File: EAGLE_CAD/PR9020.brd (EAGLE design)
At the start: 70 x 70 mm, 73 parts

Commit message: PR9020 Gerbers
PR9020 Gerbers, organized folders
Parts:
- moved MARK1 0.94 mm to (16.2, 8.50)
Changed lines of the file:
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@@
 <rectangle x1="35.3949" y1="12.6365" x2="35.4711" y2="12.6619" layer="26" rot="R180"/>
 <rectangle x1="35.4203" y1="12.6619" x2="35.5981" y2="12.6873" layer="26" rot="R180"/>
-<text x="64" y="35" size="0.8128" layer="26" font="vector" ratio="18" rot="MR270" align="center">PR9020
+<text x="64" y="35" size="0.8128" layer="26" font="vector" ratio="22" rot="MR270" align="center">PR9020
 Born + tuned in Brooklyn
 http://thepublicrad.io</text>
@@
 </element>
 <element name="R21" library="PR_Parts_Library" package="0603_CPL" value="12K" x="41.7" y="8.7" smashed="yes" rot="R180">
-<attribute name="NAME" x="43.551" y="8.389" size="0.8128" layer="25" font="vector" ratio="16"/>
+<attribute name="NAME" x="43.851" y="8.389" size="0.8128" layer="25" font="vector" ratio="16"/>
 <attribute name="VALUE" x="42.589" y="10.732" size="1.27" layer="27" rot="R180"/>
 <attribute name="MFG_PN" value="RC0603FR-0712KL" x="41.7" y="8.7" size="1.778" layer="27" rot="R180" display="off"/>
@@
 </element>
 <element name="C21" library="PR_Parts_Library" package="0603_CPL" value=".22uF" x="41.9" y="7.1" smashed="yes" rot="R180">
-<attribute name="NAME" x="43.861" y="6.762" size="0.8128" layer="25" font="vector" ratio="16"/>
+<attribute name="NAME" x="43.761" y="6.762" size="0.8128" layer="25" font="vector" ratio="16"/>
 <attribute name="VALUE" x="42.789" y="9.132" size="1.27" layer="27" rot="R180"/>
 <attribute name="MFG_PN" value="C1608X7R1C224K080AC" x="41.9" y="7.1" size="1.778" layer="27" rot="R180" display="off"/>
@@
 </element>
 <element name="C23" library="PR_Parts_Library" package="0603_CPL" value=".1uF" x="31.1" y="9.1" smashed="yes" rot="R180">
-<attribute name="NAME" x="26.8855" y="8.872" size="0.8128" layer="25" font="vector" ratio="16"/>
+<attribute name="NAME" x="27.0855" y="8.972" size="0.8128" layer="25" font="vector" ratio="16"/>
 <attribute name="VALUE" x="32.116" y="10.497" size="0.4064" layer="27" rot="R180"/>
 <attribute name="MFG_PN" value="CL10B104KB8SFNC" x="31.1" y="9.1" size="1.778" layer="27" rot="R180" display="off"/>
@@
 </element>
 <element name="FB2" library="PR_Parts_Library" package="0805_ADAFRUIT" value="" x="31.1" y="12.1" smashed="yes" rot="R180">
-<attribute name="NAME" x="26.985" y="11.88" size="0.8128" layer="25" font="vector" ratio="16"/>
+<attribute name="NAME" x="27.185" y="11.78" size="0.8128" layer="25" font="vector" ratio="16"/>
 <attribute name="VALUE" x="31.735" y="14.64" size="1.27" layer="27" rot="R180"/>
 <attribute name="MFG_PN" value="HI0805R800R-10" x="31.1" y="12.1" size="1.778" layer="27" rot="R180" display="off"/>
@@
 </element>
 <element name="FB3" library="PR_Parts_Library" package="0805_ADAFRUIT" value="" x="31.11" y="5.94" smashed="yes">
-<attribute name="NAME" x="27.275" y="5.32" size="0.8128" layer="25" font="vector" ratio="16"/>
+<attribute name="NAME" x="27.075" y="5.32" size="0.8128" layer="25" font="vector" ratio="16"/>
 <attribute name="VALUE" x="30.475" y="3.4" size="1.27" layer="27"/>
 <attribute name="MFG_PN" value="HI0805R800R-10" x="31.11" y="5.94" size="1.778" layer="27" display="off"/>
@@
 <attribute name="MFG_PN" value="DNP" x="39" y="68" size="1.778" layer="28" rot="MR0" display="off"/>
 </element>
-<element name="MARK1" library="PR_Parts_Library" package="FIDUCIAL_1MM" value="" x="17" y="9">
-<attribute name="MFG_PN" value="DNP" x="17" y="9" size="1.778" layer="27" display="off"/>
+<element name="MARK1" library="PR_Parts_Library" package="FIDUCIAL_1MM" value="" x="16.2" y="8.5">
+<attribute name="MFG_PN" value="DNP" x="16.2" y="8.5" size="1.778" layer="27" display="off"/>
 </element>
 <element name="MARK2" library="PR_Parts_Library" package="FIDUCIAL_1MM" value="" x="33" y="67">
@@
 </element>
 <element name="C24" library="PR_Parts_Library" package="0603_CPL" value="1uF" x="31.1" y="10.3" smashed="yes" rot="R180">
-<attribute name="NAME" x="27.005" y="10.565" size="0.8128" layer="25" font="vector" ratio="16"/>
+<attribute name="NAME" x="27.105" y="10.565" size="0.8128" layer="25" font="vector" ratio="16"/>
 <attribute name="VALUE" x="31.735" y="12.205" size="1.27" layer="27" rot="R180"/>
 <attribute name="MFG_PN" value="CL10B105KP8NNNC" x="31.1" y="10.3" size="1.778" layer="27" rot="R180" display="off"/>
@@
 <via x="46.35" y="40.8" extent="1-16" drill="0.6"/>
 <via x="43.15" y="4.1" extent="1-16" drill="0.6"/>
-<via x="16.09" y="6.96" extent="1-16" drill="0.6"/>
+<via x="16.79" y="6.66" extent="1-16" drill="0.6"/>
 <via x="21.8" y="13.9" extent="1-16" drill="0.6"/>
 <via x="28.55" y="23.6" extent="1-16" drill="0.6"/>

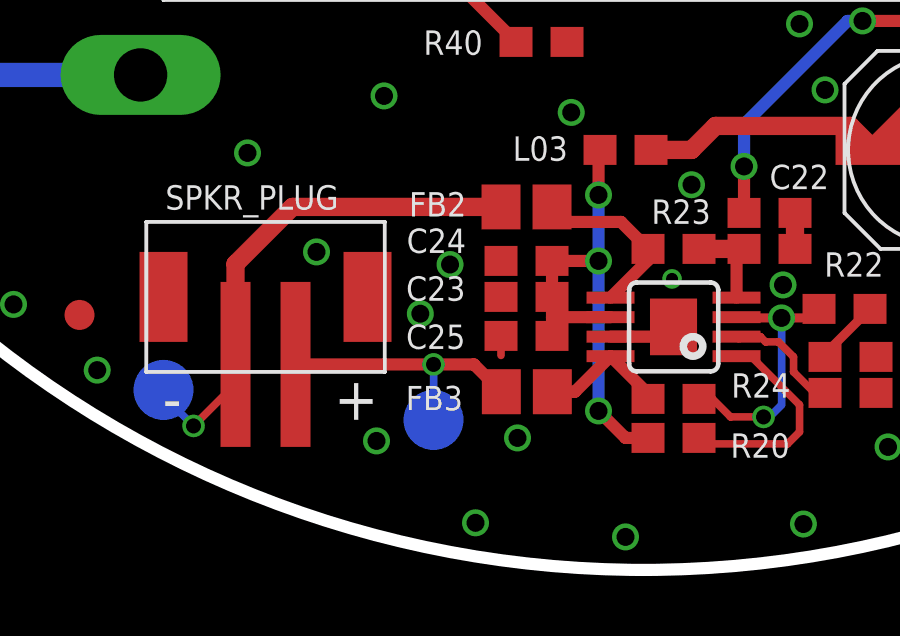
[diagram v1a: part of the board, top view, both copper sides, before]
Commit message: Updated MFG#s
Changed ferrite beads to 0 ohm resistors
Removed ‘dnp’ from R40
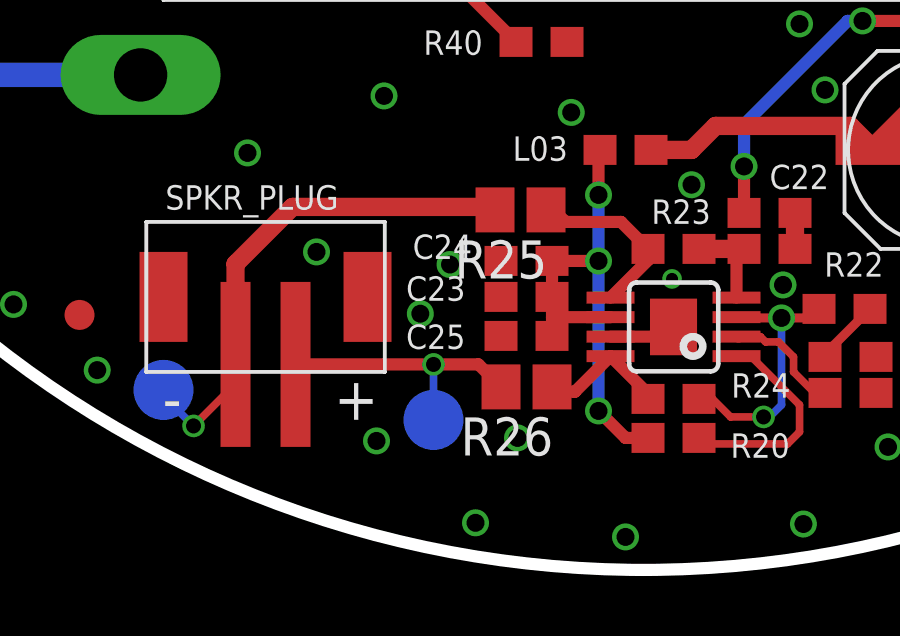
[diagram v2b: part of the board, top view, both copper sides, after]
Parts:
- removed FB2, FB3: (no value), PR_Parts_Library:0805_ADAFRUIT
- added R25, R26: 0 ohm, PR_Parts_Library:0805_ADAFRUIT
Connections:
- net N$11: now also R26.1; no longer FB3.2
- net N$4: now also R25.1; no longer FB2.1
- net SPK_OUT+: now also R25.2; no longer FB2.2
- net SPK_OUT-: now also R26.2; no longer FB3.1
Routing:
- net GND: track 16.7 -> 16.1 mm
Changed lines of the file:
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@@
 <?xml version="1.0" encoding="utf-8"?>
 <!DOCTYPE eagle SYSTEM "eagle.dtd">
-<eagle version="6.6.0">
+<eagle version="7.2.0">
 <drawing>
 <settings>
@@
 <pass name="Default">
 <param name="RoutingGrid" value="50mil"/>
+<param name="AutoGrid" value="1"/>
+<param name="Efforts" value="0"/>
+<param name="TopRouterVariant" value="1"/>
 <param name="tpViaShape" value="round"/>
 <param name="PrefDir.1" value="|"/>
@@
 <attribute name="MFG_PN" value="2 of BK92 - supplied by CL Labs" x="35" y="16.5" size="1.778" layer="28" rot="MR0" display="off"/>
 </element>
-<element name="FB2" library="PR_Parts_Library" package="0805_ADAFRUIT" value="" x="31.1" y="12.1" smashed="yes" rot="R180">
-<attribute name="NAME" x="27.185" y="11.78" size="0.8128" layer="25" font="vector" ratio="16"/>
-<attribute name="VALUE" x="31.735" y="14.64" size="1.27" layer="27" rot="R180"/>
-<attribute name="MFG_PN" value="HI0805R800R-10" x="31.1" y="12.1" size="1.778" layer="27" rot="R180" display="off"/>
-<attribute name="CURRENT" value="2A" x="31.1" y="12.1" size="1.778" layer="27" rot="R180" display="off"/>
-<attribute name="TOL" value="" x="31.1" y="12.1" size="1.778" layer="27" rot="R180" display="off"/>
-<attribute name="DCR" value="45m" x="31.1" y="12.1" size="1.778" layer="27" rot="R180" display="off"/>
-</element>
-<element name="FB3" library="PR_Parts_Library" package="0805_ADAFRUIT" value="" x="31.11" y="5.94" smashed="yes">
-<attribute name="NAME" x="27.075" y="5.32" size="0.8128" layer="25" font="vector" ratio="16"/>
-<attribute name="VALUE" x="30.475" y="3.4" size="1.27" layer="27"/>
-<attribute name="MFG_PN" value="HI0805R800R-10" x="31.11" y="5.94" size="1.778" layer="27" display="off"/>
-<attribute name="CURRENT" value="2A" x="31.11" y="5.94" size="1.778" layer="27" display="off"/>
-<attribute name="TOL" value="" x="31.11" y="5.94" size="1.778" layer="27" display="off"/>
-<attribute name="DCR" value="45m" x="31.11" y="5.94" size="1.778" layer="27" display="off"/>
-</element>
 <element name="R30" library="PR_Parts_Library" package="0603_CPL" value="10K" x="47.3" y="52" smashed="yes">
 <attribute name="NAME" x="49.111" y="51.089" size="0.8128" layer="25" font="vector" ratio="16"/>
@@
 </element>
 <element name="C24" library="PR_Parts_Library" package="0603_CPL" value="1uF" x="31.1" y="10.3" smashed="yes" rot="R180">
-<attribute name="NAME" x="27.105" y="10.565" size="0.8128" layer="25" font="vector" ratio="16"/>
+<attribute name="NAME" x="27.305" y="10.365" size="0.8128" layer="25" font="vector" ratio="16"/>
 <attribute name="VALUE" x="31.735" y="12.205" size="1.27" layer="27" rot="R180"/>
 <attribute name="MFG_PN" value="CL10B105KP8NNNC" x="31.1" y="10.3" size="1.778" layer="27" rot="R180" display="off"/>
@@
 <attribute name="VALUE" x="61.66" y="51.27" size="1.27" layer="27" rot="R270"/>
 <attribute name="MFG_PN" value="LY R976-PS-36" x="64.2" y="50" size="1.778" layer="27" rot="R180" display="off"/>
+</element>
+<element name="R25" library="PR_Parts_Library" package="0805_ADAFRUIT" value="0 ohm" x="30.9" y="12" rot="R180">
+<attribute name="TOL" value="" x="30.9" y="12" size="1.778" layer="27" rot="R180" display="off"/>
+<attribute name="MFG_PN" value="ERJ-6GEY0R00V
+" x="30.9" y="12" size="1.778" layer="27" rot="R180" display="off"/>
+<attribute name="POWER" value="" x="30.9" y="12" size="1.778" layer="27" rot="R180" display="off"/>
+</element>
+<element name="R26" library="PR_Parts_Library" package="0805_ADAFRUIT" value="0 ohm" x="31.1" y="6.1" rot="R180">
+<attribute name="TOL" value="" x="31.1" y="6.1" size="1.778" layer="27" rot="R180" display="off"/>
+<attribute name="MFG_PN" value="ERJ-6GEY0R00V
+" x="31.1" y="6.1" size="1.778" layer="27" rot="R180" display="off"/>
+<attribute name="POWER" value="" x="31.1" y="6.1" size="1.778" layer="27" rot="R180" display="off"/>
 </element>
 </elements>
@@
 <wire x1="26.65" y1="56.45" x2="26.55" y2="56.55" width="0.254" layer="1"/>
 <via x="39.65" y="9.5" extent="1-16" drill="0.6"/>
-<wire x1="30.25" y1="7.15" x2="30.25" y2="7.8" width="0.254" layer="1"/>
+<wire x1="30.25" y1="7.75" x2="30.25" y2="7.8" width="0.254" layer="1"/>
 <via x="26.1" y="4.3" extent="1-16" drill="0.6"/>
 <via x="27.56" y="8.54" extent="1-16" drill="0.6"/>
@@
 <signal name="SPK_OUT+">
 <contactref element="T6" pad="TP"/>
-<contactref element="FB2" pad="2"/>
 <contactref element="SPKR_PLUG" pad="2"/>
-<wire x1="30.25" y1="12.1" x2="23.3" y2="12.1" width="0.6096" layer="1"/>
 <wire x1="23.3" y1="12.1" x2="21.4" y2="10.2" width="0.6096" layer="1"/>
 <wire x1="21.4" y1="10.2" x2="21.4" y2="6.85" width="0.6096" layer="1"/>
@@
 <wire x1="20" y1="4.8" x2="21.4" y2="6.2" width="0.254" layer="1"/>
 <wire x1="21.4" y1="6.2" x2="21.4" y2="6.85" width="0.254" layer="1"/>
+<contactref element="R25" pad="2"/>
+<wire x1="30.05" y1="12" x2="29.95" y2="12.1" width="0.4064" layer="1"/>
+<wire x1="29.95" y1="12.1" x2="23.3" y2="12.1" width="0.6096" layer="1"/>
 </signal>
 <signal name="SPK_OUT-">
 <contactref element="T7" pad="TP"/>
-<contactref element="FB3" pad="1"/>
 <contactref element="SPKR_PLUG" pad="1"/>
-<wire x1="29.35" y1="6.85" x2="30.26" y2="5.94" width="0.4064" layer="1"/>
-<wire x1="29.35" y1="6.85" x2="28" y2="6.85" width="0.4064" layer="1"/>
 <via x="28" y="6.85" extent="1-16" drill="0.5"/>
 <wire x1="28" y1="6.85" x2="28" y2="5" width="0.254" layer="16"/>
 <wire x1="28" y1="6.85" x2="23.4" y2="6.85" width="0.4064" layer="1"/>
+<contactref element="R26" pad="2"/>
+<wire x1="30.25" y1="6.1" x2="29.5" y2="6.85" width="0.4064" layer="1"/>
+<wire x1="29.5" y1="6.85" x2="28" y2="6.85" width="0.4064" layer="1"/>
 </signal>
 <signal name="N$9">
@@
 <signal name="N$4">
 <contactref element="AMP" pad="5"/>
-<contactref element="FB2" pad="1"/>
 <contactref element="R23" pad="2"/>
 <wire x1="35.15" y1="10.7" x2="35.15" y2="10.325" width="0.4064" layer="1"/>
@@
 <wire x1="34.25" y1="11.6" x2="32.4" y2="11.6" width="0.4064" layer="1"/>
 <wire x1="32.4" y1="11.6" x2="31.95" y2="12.05" width="0.4064" layer="1"/>
-<wire x1="31.95" y1="12.05" x2="31.95" y2="12.1" width="0.4064" layer="1"/>
+<contactref element="R25" pad="1"/>
+<wire x1="31.95" y1="12.05" x2="31.9" y2="12" width="0.4064" layer="1"/>
+<wire x1="31.9" y1="12" x2="31.75" y2="12" width="0.4064" layer="1"/>
 </signal>
 <signal name="N$11">
 <contactref element="AMP" pad="8"/>
-<contactref element="FB3" pad="2"/>
 <contactref element="R24" pad="1"/>
 <wire x1="35.15" y1="5.7" x2="35.15" y2="5.875" width="0.4064" layer="1"/>
 <wire x1="35.15" y1="5.875" x2="33.9" y2="7.125" width="0.4064" layer="1"/>
-<wire x1="33.9" y1="7.125" x2="32.715" y2="5.94" width="0.4064" layer="1"/>
-<wire x1="32.715" y1="5.94" x2="31.96" y2="5.94" width="0.4064" layer="1"/>
+<contactref element="R26" pad="1"/>
+<wire x1="32.115" y1="5.94" x2="31.955" y2="6.1" width="0.4064" layer="1"/>
+<wire x1="31.955" y1="6.1" x2="31.95" y2="6.1" width="0.4064" layer="1"/>
+<wire x1="32.115" y1="5.94" x2="32.715" y2="5.94" width="0.4064" layer="1"/>
+<wire x1="32.715" y1="5.94" x2="33.9" y2="7.125" width="0.4064" layer="1"/>
 </signal>
 </signals>
